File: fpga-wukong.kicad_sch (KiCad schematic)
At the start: 0 parts

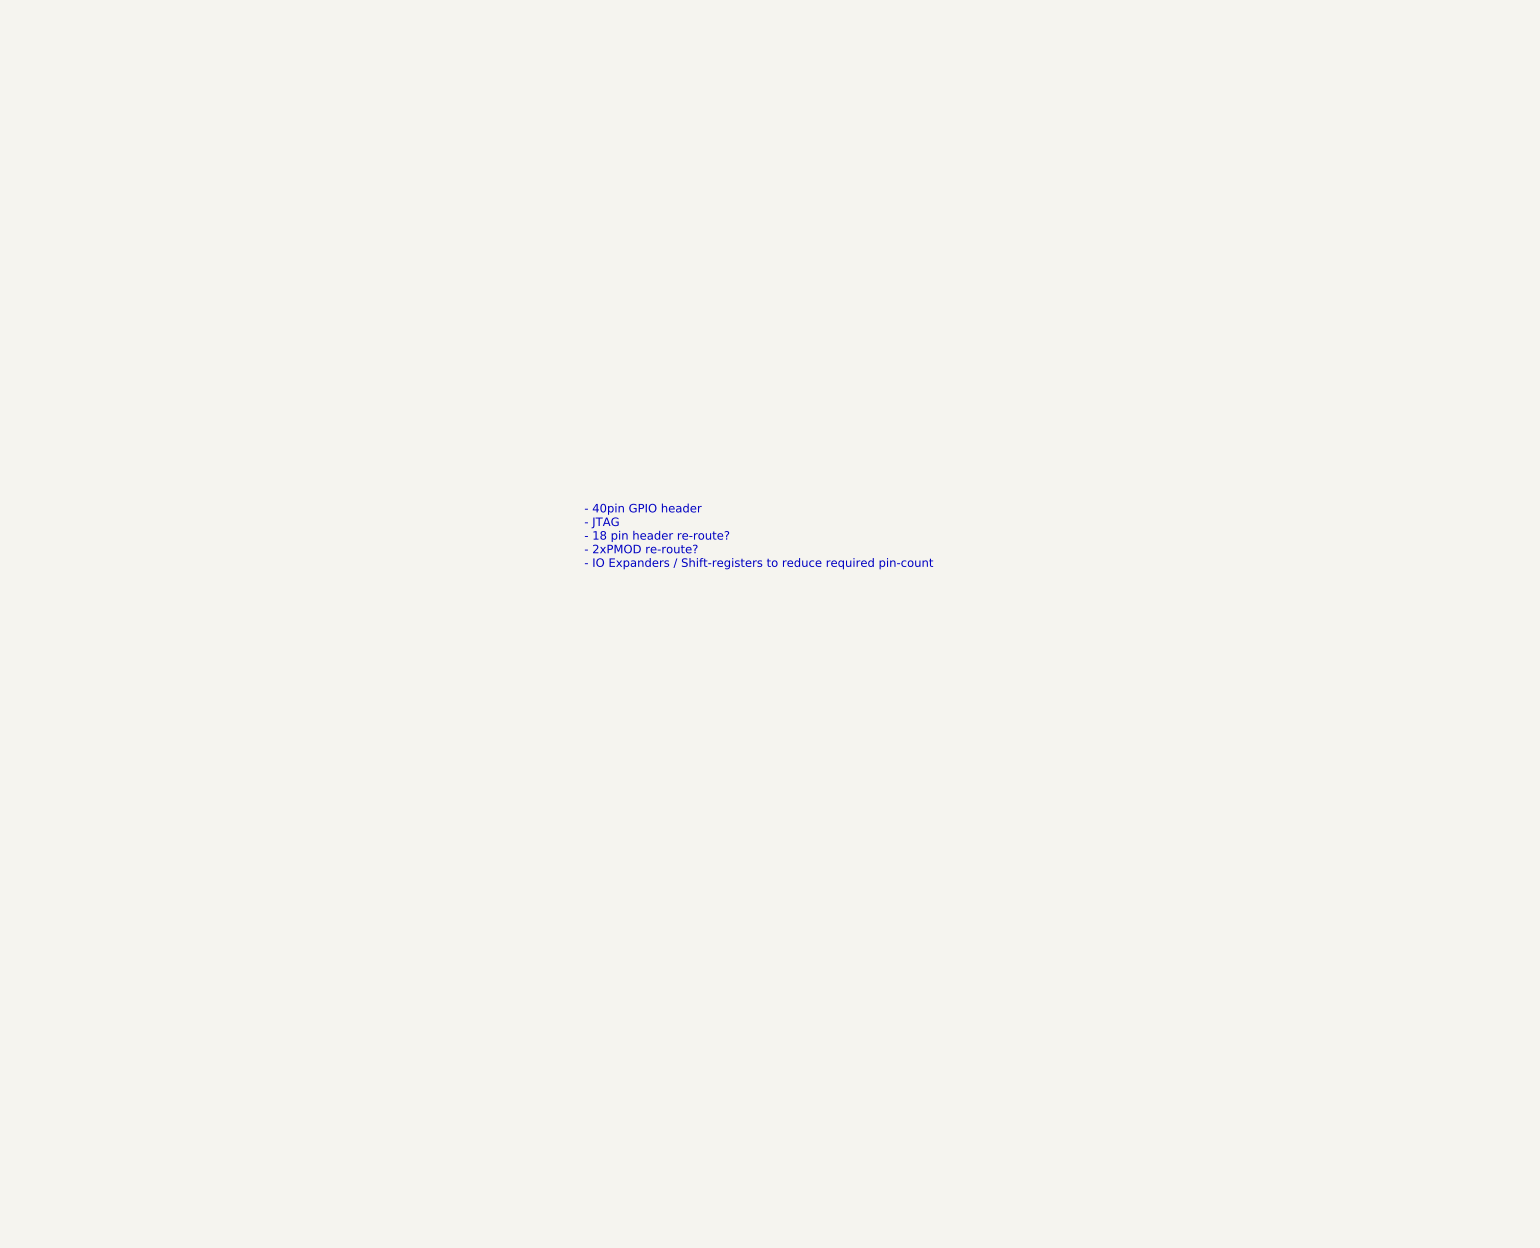
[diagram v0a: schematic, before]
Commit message: add connectors and FPGA pin descriptions for QMTECH K345T board
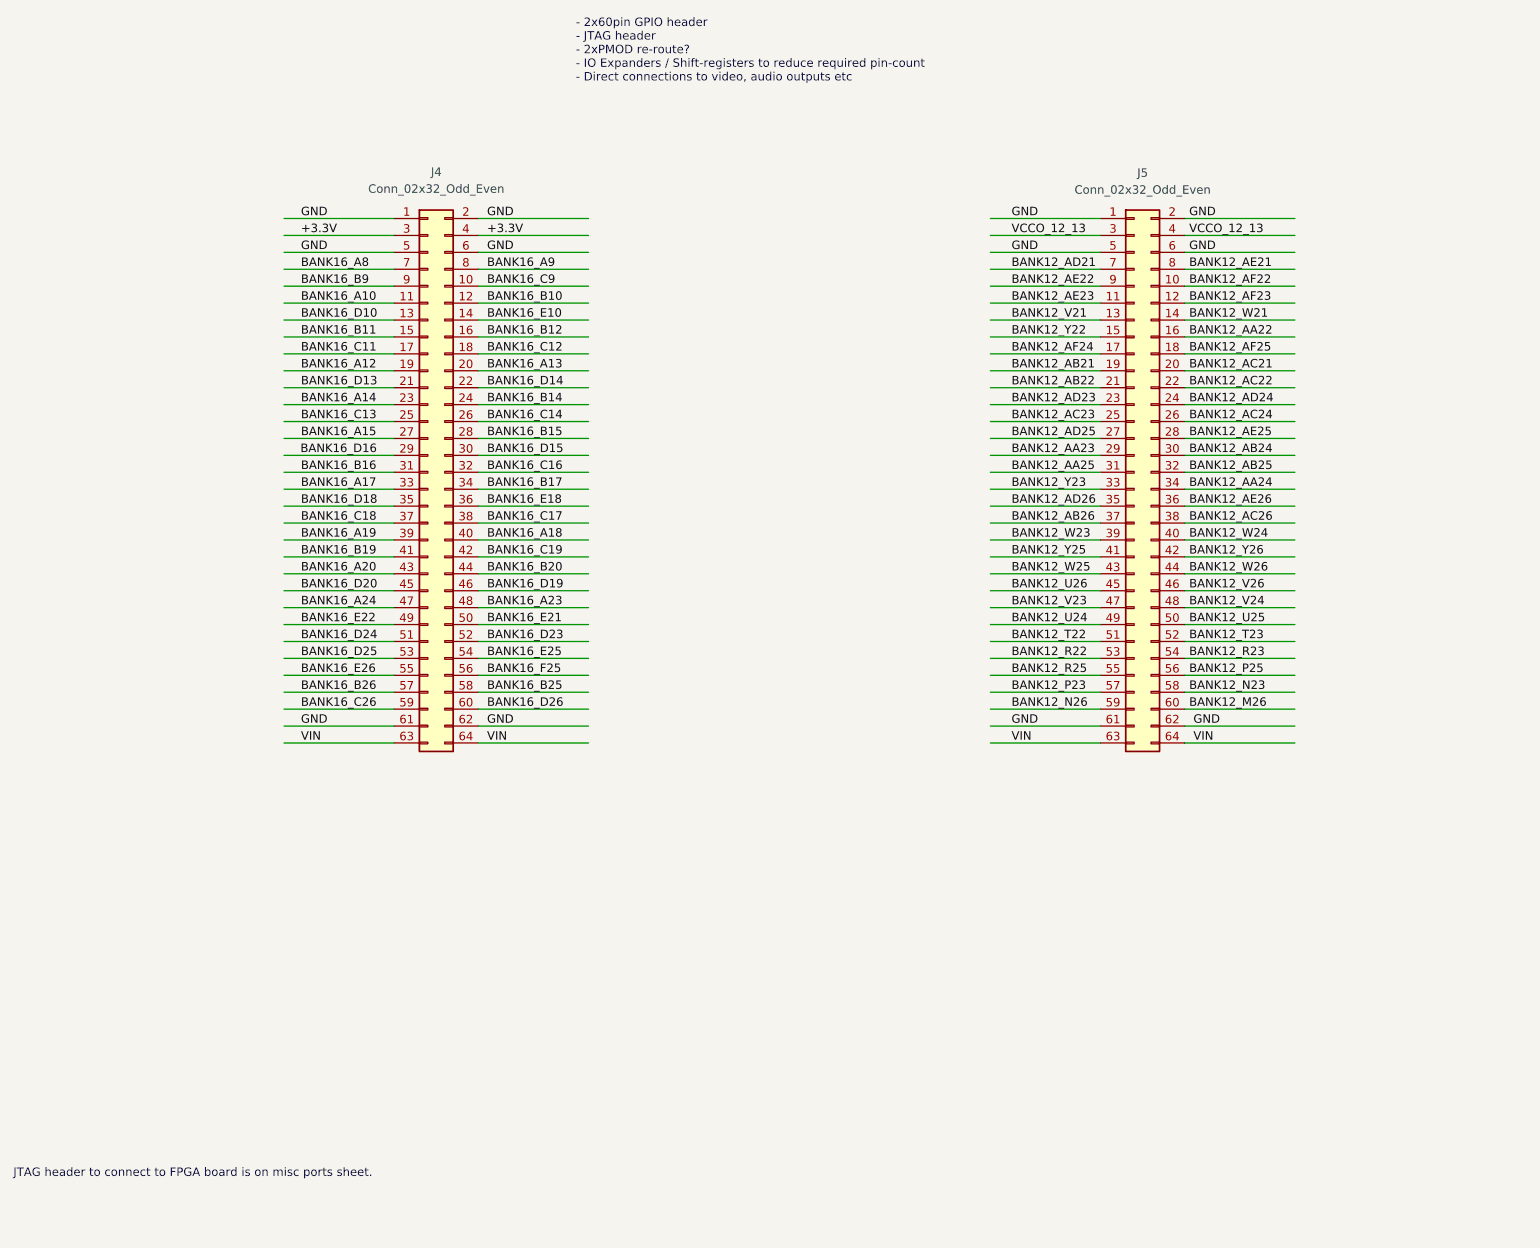
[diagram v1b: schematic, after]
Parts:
- added J4, J5: Conn_02x32_Odd_Even, symbol Connector_Generic:Conn_02x32_Odd_Even
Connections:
- new net +3.3V: J4.3 (Pin_3), J4.4 (Pin_4)
- new net BANK12_AA22: J5.16 (Pin_16)
- new net BANK12_AA23: J5.29 (Pin_29)
- new net BANK12_AA24: J5.34 (Pin_34)
- new net BANK12_AA25: J5.31 (Pin_31)
- new net BANK12_AB21: J5.19 (Pin_19)
- new net BANK12_AB22: J5.21 (Pin_21)
- new net BANK12_AB24: J5.30 (Pin_30)
- new net BANK12_AB25: J5.32 (Pin_32)
- new net BANK12_AB26: J5.37 (Pin_37)
- new net BANK12_AC21: J5.20 (Pin_20)
- new net BANK12_AC22: J5.22 (Pin_22)
- new net BANK12_AC23: J5.25 (Pin_25)
- new net BANK12_AC24: J5.26 (Pin_26)
- new net BANK12_AC26: J5.38 (Pin_38)
- new net BANK12_AD21: J5.7 (Pin_7)
- new net BANK12_AD23: J5.23 (Pin_23)
- new net BANK12_AD24: J5.24 (Pin_24)
- new net BANK12_AD25: J5.27 (Pin_27)
- new net BANK12_AD26: J5.35 (Pin_35)
- new net BANK12_AE21: J5.8 (Pin_8)
- new net BANK12_AE22: J5.9 (Pin_9)
- new net BANK12_AE23: J5.11 (Pin_11)
- new net BANK12_AE25: J5.28 (Pin_28)
- new net BANK12_AE26: J5.36 (Pin_36)
- new net BANK12_AF22: J5.10 (Pin_10)
- new net BANK12_AF23: J5.12 (Pin_12)
- new net BANK12_AF24: J5.17 (Pin_17)
- new net BANK12_AF25: J5.18 (Pin_18)
- new net BANK12_M26: J5.60 (Pin_60)
- new net BANK12_N23: J5.58 (Pin_58)
- new net BANK12_N26: J5.59 (Pin_59)
- new net BANK12_P23: J5.57 (Pin_57)
- new net BANK12_P25: J5.56 (Pin_56)
- new net BANK12_R22: J5.53 (Pin_53)
- new net BANK12_R23: J5.54 (Pin_54)
- new net BANK12_R25: J5.55 (Pin_55)
- new net BANK12_T22: J5.51 (Pin_51)
- new net BANK12_T23: J5.52 (Pin_52)
- new net BANK12_U24: J5.49 (Pin_49)
- new net BANK12_U25: J5.50 (Pin_50)
- new net BANK12_U26: J5.45 (Pin_45)
- new net BANK12_V21: J5.13 (Pin_13)
- new net BANK12_V23: J5.47 (Pin_47)
- new net BANK12_V24: J5.48 (Pin_48)
- new net BANK12_V26: J5.46 (Pin_46)
- new net BANK12_W21: J5.14 (Pin_14)
- new net BANK12_W23: J5.39 (Pin_39)
- new net BANK12_W24: J5.40 (Pin_40)
- new net BANK12_W25: J5.43 (Pin_43)
- new net BANK12_W26: J5.44 (Pin_44)
- new net BANK12_Y22: J5.15 (Pin_15)
- new net BANK12_Y23: J5.33 (Pin_33)
- new net BANK12_Y25: J5.41 (Pin_41)
- new net BANK12_Y26: J5.42 (Pin_42)
- new net BANK16_A10: J4.11 (Pin_11)
- new net BANK16_A12: J4.19 (Pin_19)
- new net BANK16_A13: J4.20 (Pin_20)
- new net BANK16_A14: J4.23 (Pin_23)
- new net BANK16_A15: J4.27 (Pin_27)
- new net BANK16_A17: J4.33 (Pin_33)
- new net BANK16_A18: J4.40 (Pin_40)
- new net BANK16_A19: J4.39 (Pin_39)
- new net BANK16_A20: J4.43 (Pin_43)
- new net BANK16_A23: J4.48 (Pin_48)
- new net BANK16_A24: J4.47 (Pin_47)
- new net BANK16_A8: J4.7 (Pin_7)
- new net BANK16_A9: J4.8 (Pin_8)
- new net BANK16_B10: J4.12 (Pin_12)
- new net BANK16_B11: J4.15 (Pin_15)
- new net BANK16_B12: J4.16 (Pin_16)
- new net BANK16_B14: J4.24 (Pin_24)
- new net BANK16_B15: J4.28 (Pin_28)
- new net BANK16_B16: J4.31 (Pin_31)
- new net BANK16_B17: J4.34 (Pin_34)
- new net BANK16_B19: J4.41 (Pin_41)
- new net BANK16_B20: J4.44 (Pin_44)
- new net BANK16_B25: J4.58 (Pin_58)
- new net BANK16_B26: J4.57 (Pin_57)
- new net BANK16_B9: J4.9 (Pin_9)
- new net BANK16_C11: J4.17 (Pin_17)
- new net BANK16_C12: J4.18 (Pin_18)
- new net BANK16_C13: J4.25 (Pin_25)
- new net BANK16_C14: J4.26 (Pin_26)
- new net BANK16_C16: J4.32 (Pin_32)
- new net BANK16_C17: J4.38 (Pin_38)
- new net BANK16_C18: J4.37 (Pin_37)
- new net BANK16_C19: J4.42 (Pin_42)
- new net BANK16_C26: J4.59 (Pin_59)
- new net BANK16_C9: J4.10 (Pin_10)
- new net BANK16_D10: J4.13 (Pin_13)
- new net BANK16_D13: J4.21 (Pin_21)
- new net BANK16_D14: J4.22 (Pin_22)
- new net BANK16_D15: J4.30 (Pin_30)
- new net BANK16_D16: J4.29 (Pin_29)
- new net BANK16_D18: J4.35 (Pin_35)
- new net BANK16_D19: J4.46 (Pin_46)
- new net BANK16_D20: J4.45 (Pin_45)
- new net BANK16_D23: J4.52 (Pin_52)
- new net BANK16_D24: J4.51 (Pin_51)
- new net BANK16_D25: J4.53 (Pin_53)
- new net BANK16_D26: J4.60 (Pin_60)
- new net BANK16_E10: J4.14 (Pin_14)
- new net BANK16_E18: J4.36 (Pin_36)
- new net BANK16_E21: J4.50 (Pin_50)
- new net BANK16_E22: J4.49 (Pin_49)
- new net BANK16_E25: J4.54 (Pin_54)
- new net BANK16_E26: J4.55 (Pin_55)
- new net BANK16_F25: J4.56 (Pin_56)
- new net GND: J4.1 (Pin_1), J4.2 (Pin_2), J4.5 (Pin_5), J4.6 (Pin_6), J4.61 (Pin_61), J4.62 (Pin_62), J5.1 (Pin_1), J5.2 (Pin_2), J5.5 (Pin_5), J5.6 (Pin_6), J5.61 (Pin_61), J5.62 (Pin_62)
- new net VCCO_12_13: J5.3 (Pin_3), J5.4 (Pin_4)
- new net VIN: J4.63 (Pin_63), J4.64 (Pin_64), J5.63 (Pin_63), J5.64 (Pin_64)
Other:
- note added: "- 2x60pin GPIO header - JTAG header - 2xPMOD re-route? - IO Expanders / Shift-registers to reduce required pin-count - Direct connections to video, audio outputs etc"
- note added: "JTAG header to connect to FPGA board is on misc ports sheet."
- note removed: "- 40pin GPIO header - JTAG - 18 pin header re-route? - 2xPMOD re-route? - IO Expanders / Shift-registers to reduce required pin-count"

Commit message: plumb all direct FPGA signals.
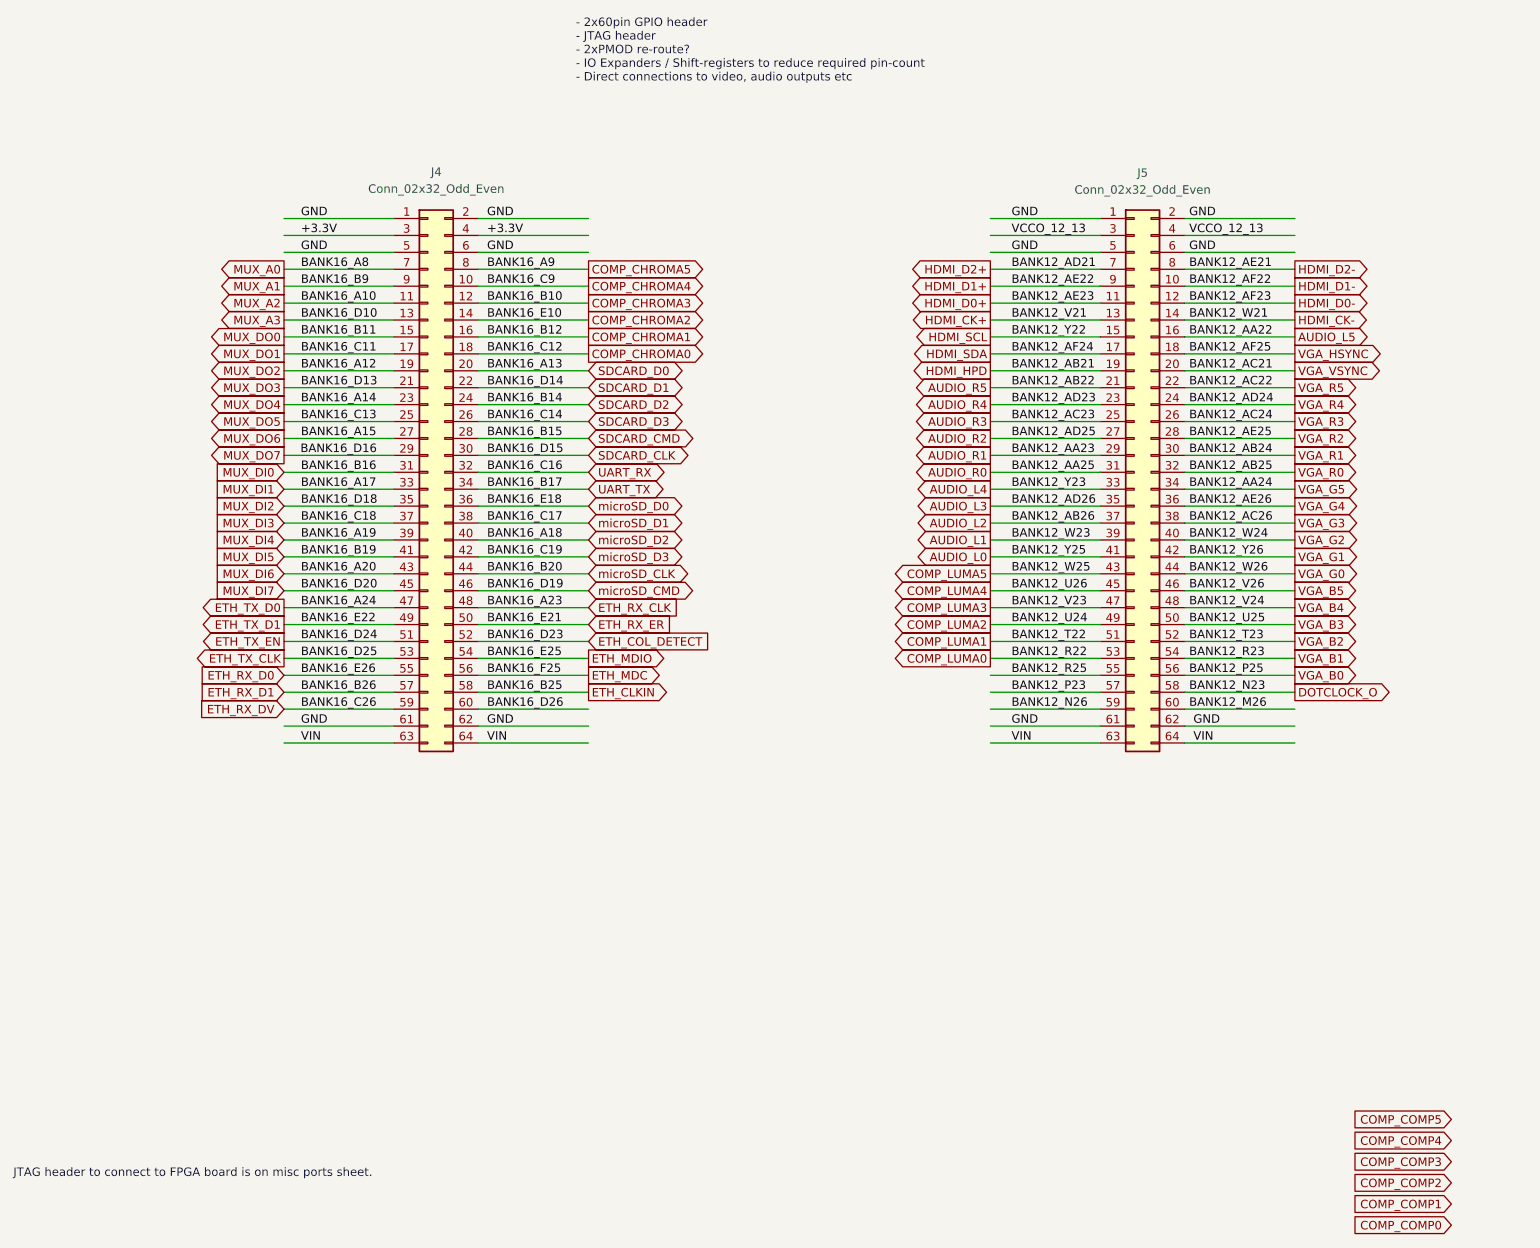
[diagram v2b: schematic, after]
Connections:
- net BANK12_AA22 renamed AUDIO_L5
- net BANK12_AA23 renamed AUDIO_R1
- net BANK12_AA24 renamed VGA_G5
- net BANK12_AA25 renamed AUDIO_R0
- net BANK12_AB21 renamed HDMI_HPD
- net BANK12_AB22 renamed AUDIO_R5
- net BANK12_AB24 renamed VGA_R1
- net BANK12_AB25 renamed VGA_R0
- net BANK12_AB26 renamed AUDIO_L2
- net BANK12_AC21 renamed VGA_VSYNC
- net BANK12_AC22 renamed VGA_R5
- net BANK12_AC23 renamed AUDIO_R3
- net BANK12_AC24 renamed VGA_R3
- net BANK12_AC26 renamed VGA_G3
- net BANK12_AD21 renamed HDMI_D2+
- net BANK12_AD23 renamed AUDIO_R4
- net BANK12_AD24 renamed VGA_R4
- net BANK12_AD25 renamed AUDIO_R2
- net BANK12_AD26 renamed AUDIO_L3
- net BANK12_AE21 renamed HDMI_D2-
- net BANK12_AE22 renamed HDMI_D1+
- net BANK12_AE23 renamed HDMI_D0+
- net BANK12_AE25 renamed VGA_R2
- net BANK12_AE26 renamed VGA_G4
- net BANK12_AF22 renamed HDMI_D1-
- net BANK12_AF23 renamed HDMI_D0-
- net BANK12_AF24 renamed HDMI_SDA
- net BANK12_AF25 renamed VGA_HSYNC
- net BANK12_N23 renamed DOTCLOCK_O
- net BANK12_P25 renamed VGA_B0
- net BANK12_R22 renamed COMP_LUMA0
- net BANK12_R23 renamed VGA_B1
- net BANK12_T22 renamed COMP_LUMA1
- net BANK12_T23 renamed VGA_B2
- net BANK12_U24 renamed COMP_LUMA2
- net BANK12_U25 renamed VGA_B3
- net BANK12_U26 renamed COMP_LUMA4
- net BANK12_V21 renamed HDMI_CK+
- net BANK12_V23 renamed COMP_LUMA3
- net BANK12_V24 renamed VGA_B4
- net BANK12_V26 renamed VGA_B5
- net BANK12_W21 renamed HDMI_CK-
- net BANK12_W23 renamed AUDIO_L1
- net BANK12_W24 renamed VGA_G2
- net BANK12_W25 renamed COMP_LUMA5
- net BANK12_W26 renamed VGA_G0
- net BANK12_Y22 renamed HDMI_SCL
- net BANK12_Y23 renamed AUDIO_L4
- net BANK12_Y25 renamed AUDIO_L0
- net BANK12_Y26 renamed VGA_G1
- net BANK16_A10 renamed MUX_A2
- net BANK16_A12 renamed MUX_DO2
- net BANK16_A13 renamed SDCARD_D0
- net BANK16_A14 renamed MUX_DO4
- net BANK16_A15 renamed MUX_DO6
- net BANK16_A17 renamed MUX_DI1
- net BANK16_A18 renamed microSD_D2
- net BANK16_A19 renamed MUX_DI4
- net BANK16_A20 renamed MUX_DI6
- net BANK16_A23 renamed ETH_RX_CLK
- net BANK16_A24 renamed ETH_TX_D0
- net BANK16_A8 renamed MUX_A0
- net BANK16_A9 renamed COMP_CHROMA5
- net BANK16_B10 renamed COMP_CHROMA3
- net BANK16_B11 renamed MUX_DO0
- net BANK16_B12 renamed COMP_CHROMA1
- net BANK16_B14 renamed SDCARD_D2
- net BANK16_B15 renamed SDCARD_CMD
- net BANK16_B16 renamed MUX_DI0
- net BANK16_B17 renamed UART_TX
- net BANK16_B19 renamed MUX_DI5
- net BANK16_B20 renamed microSD_CLK
- net BANK16_B25 renamed ETH_CLKIN
- net BANK16_B26 renamed ETH_RX_D1
- net BANK16_B9 renamed MUX_A1
- net BANK16_C11 renamed MUX_DO1
- net BANK16_C12 renamed COMP_CHROMA0
- net BANK16_C13 renamed MUX_DO5
- net BANK16_C14 renamed SDCARD_D3
- net BANK16_C16 renamed UART_RX
- net BANK16_C17 renamed microSD_D1
- net BANK16_C18 renamed MUX_DI3
- net BANK16_C19 renamed microSD_D3
- net BANK16_C26 renamed ETH_RX_DV
- net BANK16_C9 renamed COMP_CHROMA4
- net BANK16_D10 renamed MUX_A3
- net BANK16_D13 renamed MUX_DO3
- net BANK16_D14 renamed SDCARD_D1
- net BANK16_D15 renamed SDCARD_CLK
- net BANK16_D16 renamed MUX_DO7
- net BANK16_D18 renamed MUX_DI2
- net BANK16_D19 renamed microSD_CMD
- net BANK16_D20 renamed MUX_DI7
- net BANK16_D23 renamed ETH_COL_DETECT
- net BANK16_D24 renamed ETH_TX_EN
- net BANK16_D25 renamed ETH_TX_CLK
- net BANK16_E10 renamed COMP_CHROMA2
- net BANK16_E18 renamed microSD_D0
- net BANK16_E21 renamed ETH_RX_ER
- net BANK16_E22 renamed ETH_TX_D1
- net BANK16_E25 renamed ETH_MDIO
- net BANK16_E26 renamed ETH_RX_D0
- net BANK16_F25 renamed ETH_MDC
